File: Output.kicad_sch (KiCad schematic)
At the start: 16 parts, among them U401 74HC157, U402 74HC365

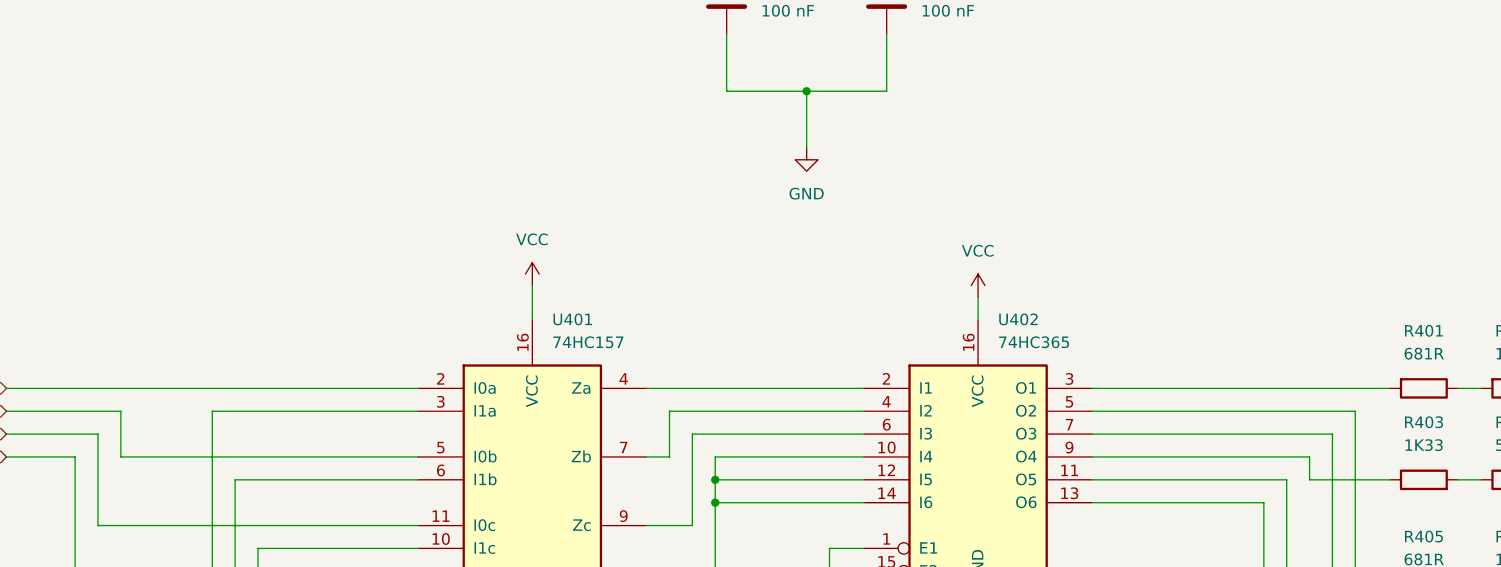
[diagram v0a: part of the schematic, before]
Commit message: chips driven by GAL or memory need to be 74HCT
I forgot that GALs only guarantee 2.4V as the minimum
output high voltage. Bleh.
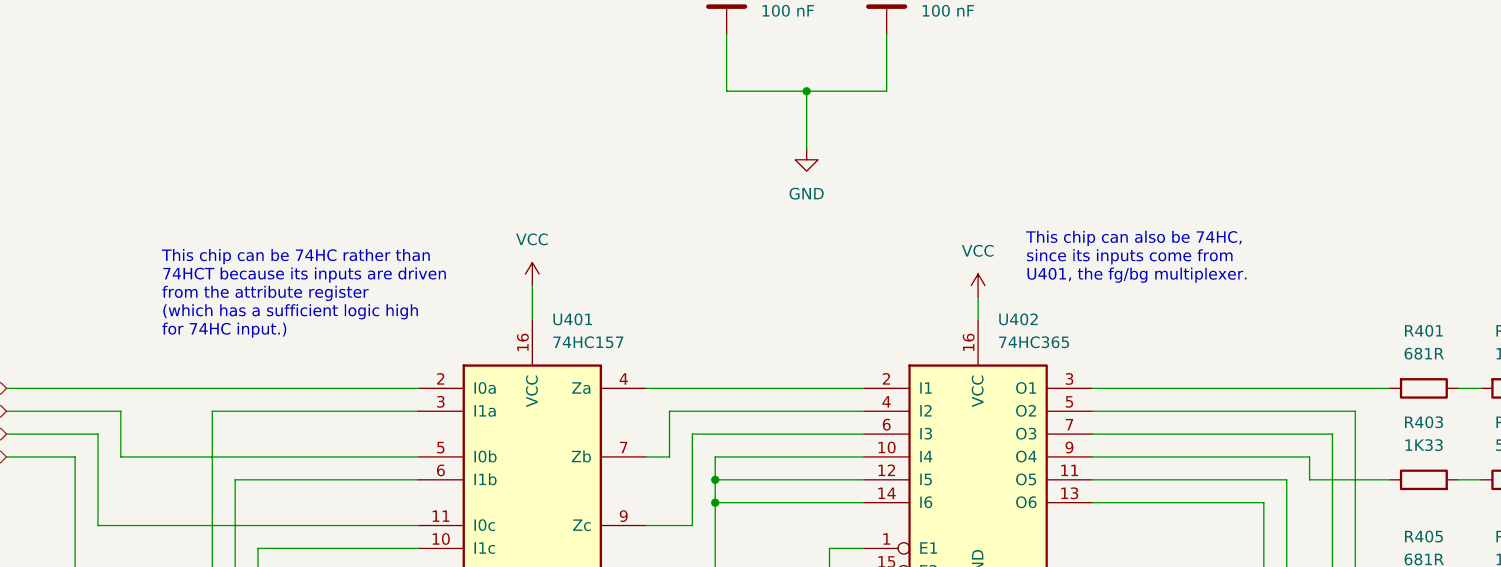
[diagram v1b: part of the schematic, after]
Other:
- note added: "This chip can also be 74HC, since its inputs come from U401, the fg/bg multiplexer."
- note added: "This chip can be 74HC rather than 74HCT because its inputs are driven from the attribute register (which has a sufficient logic high for 74HC input.)"
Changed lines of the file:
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@@
+		)
+	)
+	(text "This chip can be 74HC rather than\n74HCT because its inputs are driven\nfrom the attribute register\n(which has a sufficient logic high\nfor 74HC input.)"
+		(exclude_from_sim no)
+		(at 56.642 70.866 0)
+		(effects
+			(font
+				(size 1.27 1.27)
+			)
+			(justify left)
 		)
 	)
@@
 		(effects
 			(font
+				(size 1.27 1.27)
+			)
+			(justify left)
+		)
+	)
+	(text "This chip can also be 74HC,\nsince its inputs come from\nU401, the fg/bg multiplexer."
+		(exclude_from_sim no)
+		(at 152.654 66.802 0)
+		(effects
+			(font

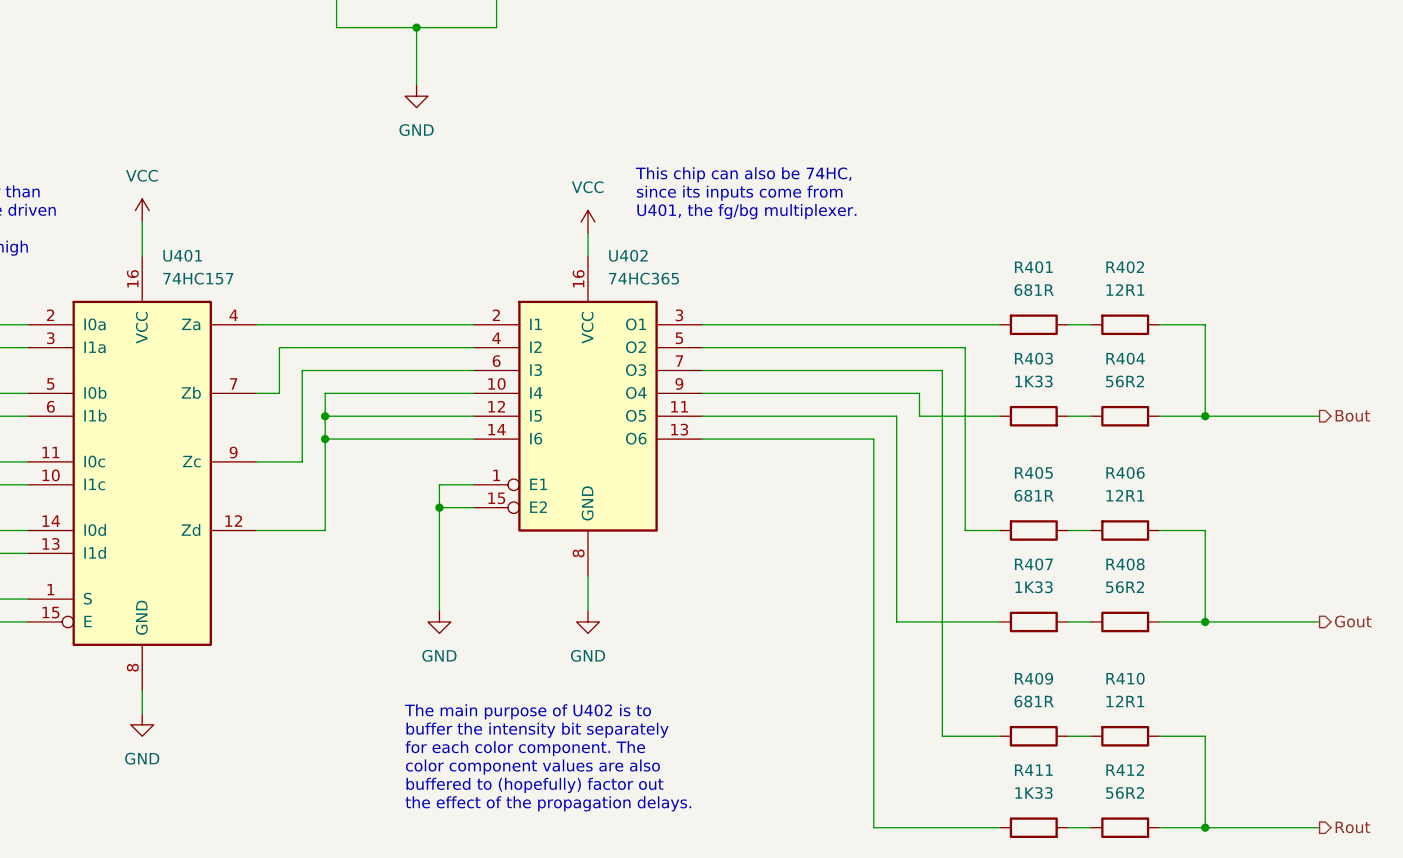
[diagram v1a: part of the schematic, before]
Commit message: use 74ACT parts where needed (e.g., HCount)
Also, I don't think the 74HCT365 buffer is needed for
the output DAC. I think a single intensity output can
feed into all three color outputs. It's a voltage source,
so it shouldn't really matter what load is on it.
(Need to test this out in simulation.)
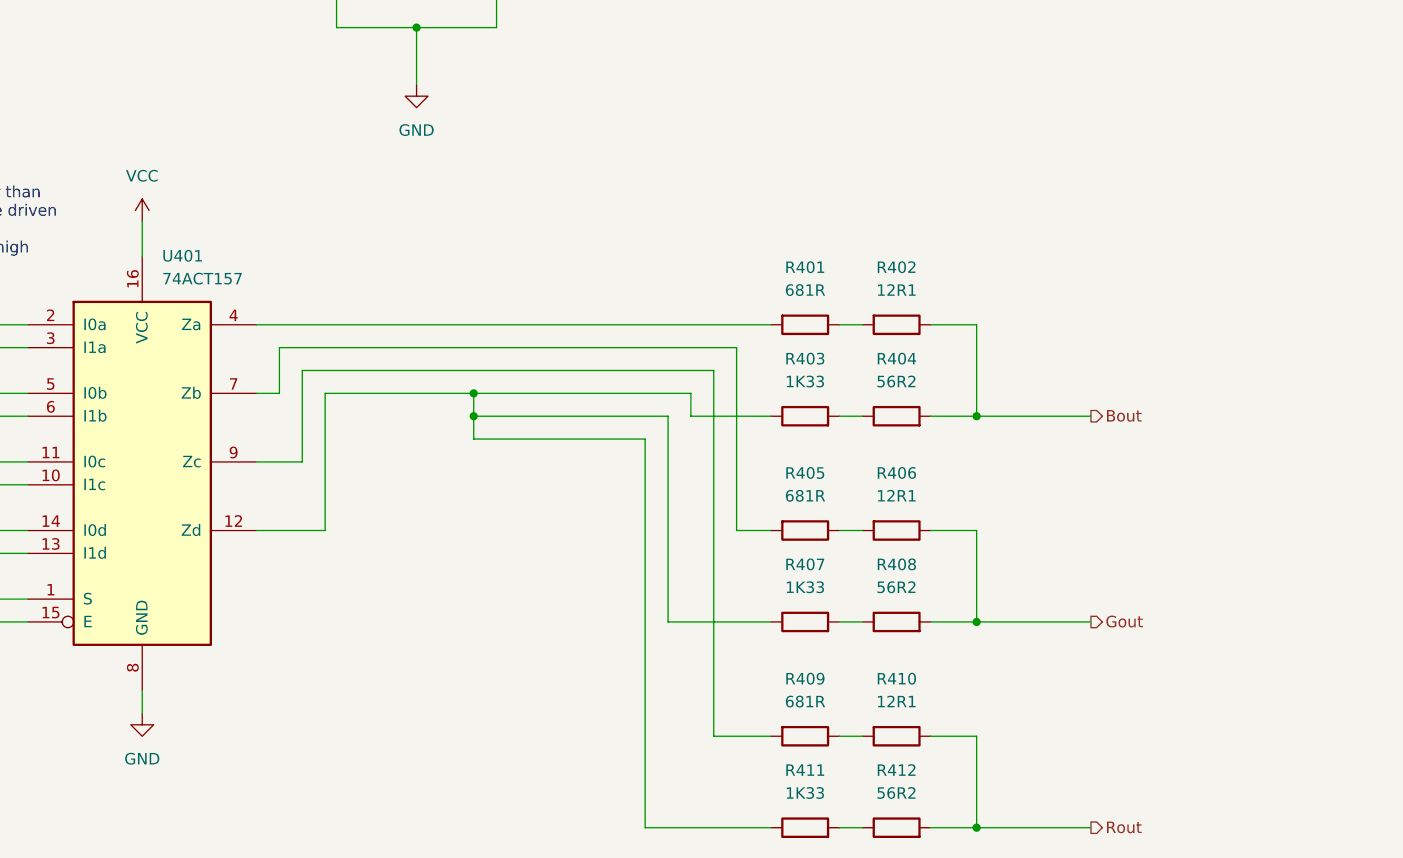
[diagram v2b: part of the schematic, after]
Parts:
- removed U402: 74HC365, symbol 74xx:74LS365
- U401: value 74HC157 -> 74ACT157
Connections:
- net at R405.2: now also U401.7 (Zb)
- net at R407.1: now also R403.1, R411.1, U401.12 (Zd)
- net at R401.2: now also U401.4 (Za)
- net at U401.9 (Zc): now also R409.2
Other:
- note removed: "The main purpose of U402 is to buffer the intensity bit separately for each color component. The color component values are also buffered to (hopefully) factor out the effect of the propagation delays."
- note removed: "This chip can also be 74HC, since its inputs come from U401, the fg/bg multiplexer."
- moved on the sheet: R401, R402, R403, R404, R405, R406, R407, R408, R409, R410, R411, R412
